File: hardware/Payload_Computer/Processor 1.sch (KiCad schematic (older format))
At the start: 1 part

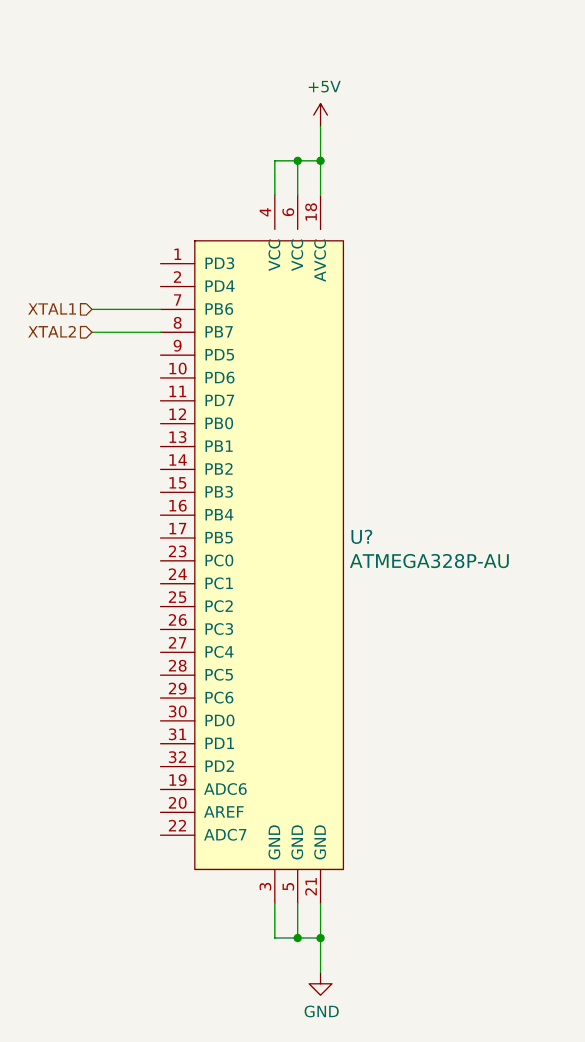
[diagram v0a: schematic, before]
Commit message: Added FTDI and crystals
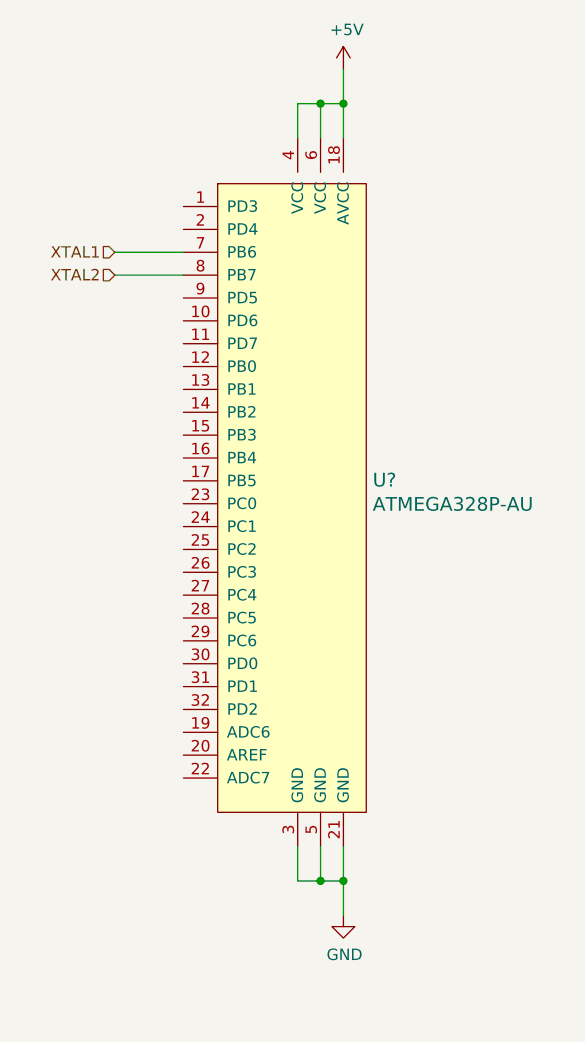
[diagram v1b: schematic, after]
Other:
- moved on the sheet: U?
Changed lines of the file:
@@
 $Descr A4 11693 8268
 encoding utf-8
-Sheet 2 3
+Sheet 2 6
 Title ""
 Date ""
@@
 L dk_Embedded-Microcontrollers:ATMEGA328P-AU U?
 U 1 1 5F845D97
-P 6450 3650
-F 0 "U?" H 6778 3753 60  0000 L CNN
-F 1 "ATMEGA328P-AU" H 6778 3647 60  0000 L CNN
-F 2 "digikey-footprints:TQFP-32_7x7mm" H 6650 3850 60  0001 L CNN
-F 3 "http://www.microchip.com/mymicrochip/filehandler.aspx?ddocname=en608326" H 6650 3950 60  0001 L CNN
-F 4 "ATMEGA328P-AU-ND" H 6650 4050 60  0001 L CNN "Digi-Key_PN"
-F 5 "ATMEGA328P-AU" H 6650 4150 60  0001 L CNN "MPN"
-F 6 "Integrated Circuits (ICs)" H 6650 4250 60  0001 L CNN "Category"
-F 7 "Embedded - Microcontrollers" H 6650 4350 60  0001 L CNN "Family"
-F 8 "http://www.microchip.com/mymicrochip/filehandler.aspx?ddocname=en608326" H 6650 4450 60  0001 L CNN "DK_Datasheet_Link"
-F 9 "/product-detail/en/microchip-technology/ATMEGA328P-AU/ATMEGA328P-AU-ND/1832260" H 6650 4550 60  0001 L CNN "DK_Detail_Page"
-F 10 "IC MCU 8BIT 32KB FLASH 32TQFP" H 6650 4650 60  0001 L CNN "Description"
-F 11 "Microchip Technology" H 6650 4750 60  0001 L CNN "Manufacturer"
-F 12 "Active" H 6650 4850 60  0001 L CNN "Status"
-	1    6450 3650
+P 6550 3400
+F 0 "U?" H 6878 3503 60  0000 L CNN
+F 1 "ATMEGA328P-AU" H 6878 3397 60  0000 L CNN
+F 2 "digikey-footprints:TQFP-32_7x7mm" H 6750 3600 60  0001 L CNN
+F 3 "http://www.microchip.com/mymicrochip/filehandler.aspx?ddocname=en608326" H 6750 3700 60  0001 L CNN
+F 4 "ATMEGA328P-AU-ND" H 6750 3800 60  0001 L CNN "Digi-Key_PN"
+F 5 "ATMEGA328P-AU" H 6750 3900 60  0001 L CNN "MPN"
+F 6 "Integrated Circuits (ICs)" H 6750 4000 60  0001 L CNN "Category"
+F 7 "Embedded - Microcontrollers" H 6750 4100 60  0001 L CNN "Family"
+F 8 "http://www.microchip.com/mymicrochip/filehandler.aspx?ddocname=en608326" H 6750 4200 60  0001 L CNN "DK_Datasheet_Link"
+F 9 "/product-detail/en/microchip-technology/ATMEGA328P-AU/ATMEGA328P-AU-ND/1832260" H 6750 4300 60  0001 L CNN "DK_Detail_Page"
+F 10 "IC MCU 8BIT 32KB FLASH 32TQFP" H 6750 4400 60  0001 L CNN "Description"
+F 11 "Microchip Technology" H 6750 4500 60  0001 L CNN "Manufacturer"
+F 12 "Active" H 6750 4600 60  0001 L CNN "Status"
+	1    6550 3400
 	1    0    0    -1
 $EndComp
@@
 L power:+5V #PWR?
 U 1 1 5F848BC8
-P 6650 1750
-F 0 "#PWR?" H 6650 1600 50  0001 C CNN
-F 1 "+5V" H 6665 1923 50  0000 C CNN
-F 2 "" H 6650 1750 50  0001 C CNN
-F 3 "" H 6650 1750 50  0001 C CNN
-	1    6650 1750
+P 6750 1500
+F 0 "#PWR?" H 6750 1350 50  0001 C CNN
+F 1 "+5V" H 6765 1673 50  0000 C CNN
+F 2 "" H 6750 1500 50  0001 C CNN
+F 3 "" H 6750 1500 50  0001 C CNN
+	1    6750 1500
 	1    0    0    -1
 $EndComp
 Wire Wire Line
-	6650 2050 6650 1900
+	6750 1800 6750 1650
 Wire Wire Line
-	6550 2050 6550 1900
+	6650 1800 6650 1650
 Wire Wire Line
-	6550 1900 6650 1900
-Connection ~ 6650 1900
+	6650 1650 6750 1650
+Connection ~ 6750 1650
 Wire Wire Line
-	6650 1900 6650 1750
+	6750 1650 6750 1500
 Wire Wire Line
-	6450 2050 6450 1900
+	6550 1800 6550 1650
 Wire Wire Line
-	6450 1900 6550 1900
-Connection ~ 6550 1900
+	6550 1650 6650 1650
+Connection ~ 6650 1650
 $Comp
 L power:GND #PWR?
 U 1 1 5F84953E
-P 6650 5450
-F 0 "#PWR?" H 6650 5200 50  0001 C CNN
-F 1 "GND" H 6655 5277 50  0000 C CNN
-F 2 "" H 6650 5450 50  0001 C CNN
-F 3 "" H 6650 5450 50  0001 C CNN
-	1    6650 5450
+P 6750 5200
+F 0 "#PWR?" H 6750 4950 50  0001 C CNN
+F 1 "GND" H 6755 5027 50  0000 C CNN
+F 2 "" H 6750 5200 50  0001 C CNN
+F 3 "" H 6750 5200 50  0001 C CNN
+	1    6750 5200
 	1    0    0    -1
 $EndComp
 Wire Wire Line
-	6650 5150 6650 5300
+	6750 4900 6750 5050
 Wire Wire Line
-	6550 5150 6550 5300
+	6650 4900 6650 5050
 Wire Wire Line
-	6550 5300 6650 5300
-Connection ~ 6650 5300
+	6650 5050 6750 5050
+Connection ~ 6750 5050
 Wire Wire Line
-	6650 5300 6650 5450
+	6750 5050 6750 5200
 Wire Wire Line
-	6450 5150 6450 5300
+	6550 4900 6550 5050
 Wire Wire Line
-	6450 5300 6550 5300
-Connection ~ 6550 5300
-Text HLabel 5650 2550 0    50   Input ~ 0
+	6550 5050 6650 5050
+Connection ~ 6650 5050
+Text HLabel 5750 2300 0    50   Input ~ 0
 XTAL1
-Text HLabel 5650 2650 0    50   Input ~ 0
+Text HLabel 5750 2400 0    50   Input ~ 0
 XTAL2
 Wire Wire Line
-	5650 2550 5950 2550
+	5750 2300 6050 2300
 Wire Wire Line
-	5650 2650 5950 2650
+	5750 2400 6050 2400
 $EndSCHEMATC

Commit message: Minor updates to FTDI
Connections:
- net RESET: now reaches U?.29 (PC6)
- net RXD: now reaches U?.30 (PD0)
- net TXD: now reaches U?.31 (PD1)
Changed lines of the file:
@@
 Wire Wire Line
 	5750 2400 6050 2400
+Text HLabel 5750 4200 0    50   Input ~ 0
+TXD
+Text HLabel 5750 4100 0    50   Input ~ 0
+RXD
+Wire Wire Line
+	5750 4100 6050 4100
+Wire Wire Line
+	5750 4200 6050 4200
+Text HLabel 5750 4000 0    50   Input ~ 0
+RESET
+Wire Wire Line
+	5750 4000 6050 4000
 $EndSCHEMATC

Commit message: Finished ICSP. Added a few leds and filtering caps
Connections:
- net MOSI: now reaches U?.15 (PB3)
- net MISO: now reaches U?.16 (PB4)
- net SCK: now reaches U?.17 (PB5)
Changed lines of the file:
@@
 $Descr A4 11693 8268
 encoding utf-8
-Sheet 2 11
+Sheet 2 13
 Title ""
 Date ""
@@
 $EndComp
 $Comp
-L power:+5V #PWR?
+L power:+5V #PWR0101
 U 1 1 5F848BC8
 P 6750 1500
-F 0 "#PWR?" H 6750 1350 50  0001 C CNN
+F 0 "#PWR0101" H 6750 1350 50  0001 C CNN
 F 1 "+5V" H 6765 1673 50  0000 C CNN
 F 2 "" H 6750 1500 50  0001 C CNN
@@
 Connection ~ 6650 1650
 $Comp
-L power:GND #PWR?
+L power:GND #PWR0102
 U 1 1 5F84953E
 P 6750 5200
-F 0 "#PWR?" H 6750 4950 50  0001 C CNN
+F 0 "#PWR0102" H 6750 4950 50  0001 C CNN
 F 1 "GND" H 6755 5027 50  0000 C CNN
 F 2 "" H 6750 5200 50  0001 C CNN
@@
 Wire Wire Line
 	5750 4000 6050 4000
+Text HLabel 5750 3100 0    50   Input ~ 0
+MOSI
+Text HLabel 5750 3200 0    50   Input ~ 0
+MISO
+Text HLabel 5750 3300 0    50   Input ~ 0
+SCK
+Wire Wire Line
+	5750 3100 6050 3100
+Wire Wire Line
+	6050 3200 5750 3200
+Wire Wire Line
+	5750 3300 6050 3300
 $EndSCHEMATC
